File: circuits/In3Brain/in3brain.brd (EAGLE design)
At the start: 42.2 x 38.2 mm, 21 parts, among them IC1 ATMEGA48/88/168-AU, IC2 REG1117

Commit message: Electronics v2
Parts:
- removed LED: (no value), ng:1206
- removed R9: 0, ng:1206
- removed S1: (no value), ng:6MM_SWITCH
- removed SV2, SV3: (no value), con-lstb:MA06-1
- added J1: JACK.65MM, 01_fab:JACK_.65MM
- added SV5, SV6: (no value), con-lstb:MA05-2
- R1: value 10k -> 0
- R2: value 499 -> 0
- SL1: device con-amp-quick:02PA -> con-amp-quick:05PA
- moved R8 48.7 mm to (49.9, 59.4), turned to 0 degrees
- moved R4 44.2 mm to (43.3, 59.6)
- moved SL1 41.1 mm to (40.3, 66.1)
- moved C2 39.9 mm to (55.6, 45.5), turned to 0 degrees
- moved R3 39.6 mm to (41.7, 62.5), turned to 180 degrees
- moved R7 38.5 mm to (55.7, 41.2)
- moved U$1 37.5 mm to (53.2, 35.3)
- moved C5 36.4 mm to (35.5, 60.2), turned to 270 degrees
- moved IC1 35.9 mm to (40.6, 43.2)
- moved U$2 35.2 mm to (31.7, 39.4)
- moved C1 33.4 mm to (32.6, 60.0), turned to 270 degrees
- moved R2 31.2 mm to (28.7, 35.9)
- moved R1 25.5 mm to (41.5, 25.5), turned to 90 degrees
- moved C3 21.5 mm to (28.6, 30.6), turned to 0 degrees
- moved C6 17.3 mm to (28.6, 27.7), turned to 0 degrees
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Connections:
- removed net EN: SV2.1
- removed net N$23: LED.1, R2.2
- new net $1: SV5.5
- new net $2: SV5.6
- new net BTN: IC1.2, SV5.4
- new net BUZZ: IC1.12, SV6.2
- new net INT0: IC1.32, SV5.1
- new net INT1: IC1.1, SV5.2
- new net LCD4: IC1.23, SV5.8
- new net LCD5: IC1.24, SV5.10
- new net LCD6: IC1.25, SV5.9
- new net LCD7: IC1.26, SV5.7
- new net LCDE: IC1.10, SV6.3
- new net LCDRS: IC1.11, SV6.1
- new net RGBB: IC1.14, SV6.6
- new net RGBG: IC1.13, SV6.4
- net 12V: now also J1.PIN, SL1.4; no longer SL1.1, SV3.4
- net 5V: now also R2.1, R2.2, SV6.10, SV6.7; no longer R1.2, R9.1, R9.2, SV2.2, SV3.5
- net GND: now also J1.CONTACT, J1.SHUNT, R1.1, R1.2, SL1.5, SV6.5; no longer LED.2, S1.1, S1.2, SL1.2, SV2.3, SV3.6
- net RST: now also SL1.1, SV5.3, SV6.9; no longer R1.1, S1.3, S1.4, SV3.1
- net RX: no longer SV2.6
- net SCK: now also SV6.8; no longer R2.1
- net SCL: now also SL1.3; no longer SV3.3
- net SDA: now also SL1.2; no longer SV3.2
- net STATE: now also IC1.9; no longer IC1.2, SV2.4
- net TX: no longer SV2.5
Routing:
- net GND: track 119.2 -> 154.0 mm
- net 12V: track 58.7 -> 29.1 mm
- net N$23: track 28.7 -> 0.00 mm
- net SCK: track 18.0 -> 46.6 mm
- net BTN: track 0.00 -> 23.1 mm
- net LCD4: track 0.00 -> 22.8 mm
- net LCDE: track 0.00 -> 19.9 mm
- net N$3: track 18.5 -> 0.00 mm
- net RST: track 50.3 -> 68.1 mm
- net RX: track 15.5 -> 0.00 mm
- net SDA: track 35.2 -> 20.3 mm
- net TX: track 14.4 -> 0.00 mm
- net LCDRS: track 0.00 -> 14.1 mm
- net LCD5: track 0.00 -> 13.8 mm
- net INT1: track 0.00 -> 13.8 mm
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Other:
- board size 42.2 x 38.2 mm -> 40.2 x 47.7 mm
- board text removed: "+"
- board text removed: "-"
- board text removed: "3"
- board text removed: "In"

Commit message: New Electronics
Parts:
- removed J1: JACK.65MM, 01_fab:JACK_.65MM
- removed R7, R8: 0, ng:1206
- removed SV5: (no value), con-lstb:MA05-2
- added J2: (no value), con-jack:SPC4078
- added R5: 0, ng:1206
- added SL2, SL3: (no value), con-amp-quick:03P
- added SL5: (no value), con-amp-quick:07PA
- moved C5 60.1 mm to (5.59, 8.13), turned to 180 degrees
- moved C2 51.8 mm to (6.10, 30.5)
- moved SL1 50.0 mm to (38.1, 16.2), turned to 90 degrees
- moved R4 39.6 mm to (23.3, 25.3)
- moved R3 37.6 mm to (21.2, 31.0), turned to 270 degrees
- moved IC1 37.2 mm to (16.0, 15.2)
- moved U$2 36.5 mm to (7.09, 12.4)
- moved U$1 34.7 mm to (32.1, 7.70)
- moved R1 28.5 mm to (21.3, 5.33)
- moved SV6 25.1 mm to (16.3, 29.5), turned to 90 degrees
- moved C1 25.1 mm to (23.2, 36.8), turned to 0 degrees
- moved R2 24.5 mm to (25.9, 11.5), turned to 270 degrees
- moved C3 22.7 mm to (6.10, 27.4)
- moved C6 22.7 mm to (6.10, 24.6)
- moved IC2 15.7 mm to (28.5, 32.0), turned to 270 degrees
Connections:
- removed net $1: SV5.5
- removed net $2: SV5.6
- removed net LCD4: IC1.23, SV5.8
- removed net LCD5: IC1.24, SV5.10
- removed net LCD6: IC1.25, SV5.9
- removed net LCD7: IC1.26, SV5.7
- removed net LCDE: IC1.10, SV6.3
- removed net LCDRS: IC1.11, SV6.1
- removed net RGBB: IC1.14, SV6.6
- removed net RGBG: IC1.13, SV6.4
- removed net RX: IC1.30
- removed net STATE: IC1.9
- removed net TX: IC1.31
- new net FAN12: IC1.9, SL5.5
- new net FAN5: IC1.10, SL5.4
- new net LED: IC1.2, SV6.10
- new net PUMP: IC1.13, SL5.1
- new net RELAY1: IC1.11, SL5.3
- new net RELAY2: IC1.12, SL5.2
- new net TEMP1: IC1.23, SL2.1
- new net TEMP2: IC1.24, SL3.1
- net 12V: now also J2.3, SL1.5, SL5.7; no longer J1.PIN, SL1.4
- net 5V: now also SL2.3, SL3.3; no longer R8.1, R8.2, SV6.10
- net BTN: now also IC1.31, SV6.4; no longer IC1.2, SV5.4
- net BUZZ: now also IC1.30; no longer IC1.12
- net GND: now also J2.1, J2.2, R5.1, R5.2, SL1.2, SL2.2, SL3.2, SL5.6, SV6.9; no longer J1.CONTACT, J1.SHUNT, R1.1, R1.2, SL1.5, SV6.5
- net INT0: now also IC1.1, SV6.8; no longer IC1.32, SV5.1
- net INT1: now also IC1.32, SV6.6; no longer IC1.1, SV5.2
- net MISO: now also R1.1, R1.2
- net RST: now also IC1.19, SV6.1; no longer R7.1, R7.2, SV5.3, SV6.9
- net SCK: no longer SV6.8
- net SCL: now also SV6.3
- net SDA: now also SL1.4, SV6.5; no longer SL1.2
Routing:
- net GND: track 154.0 -> 0.00 mm
- net 12V: track 29.1 -> 111.4 mm
- net 5V: track 157.2 -> 98.2 mm
- net RST: track 68.1 -> 34.7 mm
- net SCK: track 46.6 -> 16.8 mm
- net SCL: track 19.7 -> 43.1 mm
- net LCD4: track 22.8 -> 0.00 mm
- net LED: track 0.00 -> 22.2 mm
- net SDA: track 20.3 -> 42.5 mm
- net LCDE: track 19.9 -> 0.00 mm
- net TEMP2: track 0.00 -> 15.9 mm
- net BTN: track 23.1 -> 8.37 mm
- net LCDRS: track 14.1 -> 0.00 mm
- net LCD5: track 13.8 -> 0.00 mm
- net MOSI: track 11.5 -> 24.5 mm
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- added copper zone on layer 1, net GND
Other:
- board size 40.2 x 47.7 mm -> 50.5 x 46.5 mm

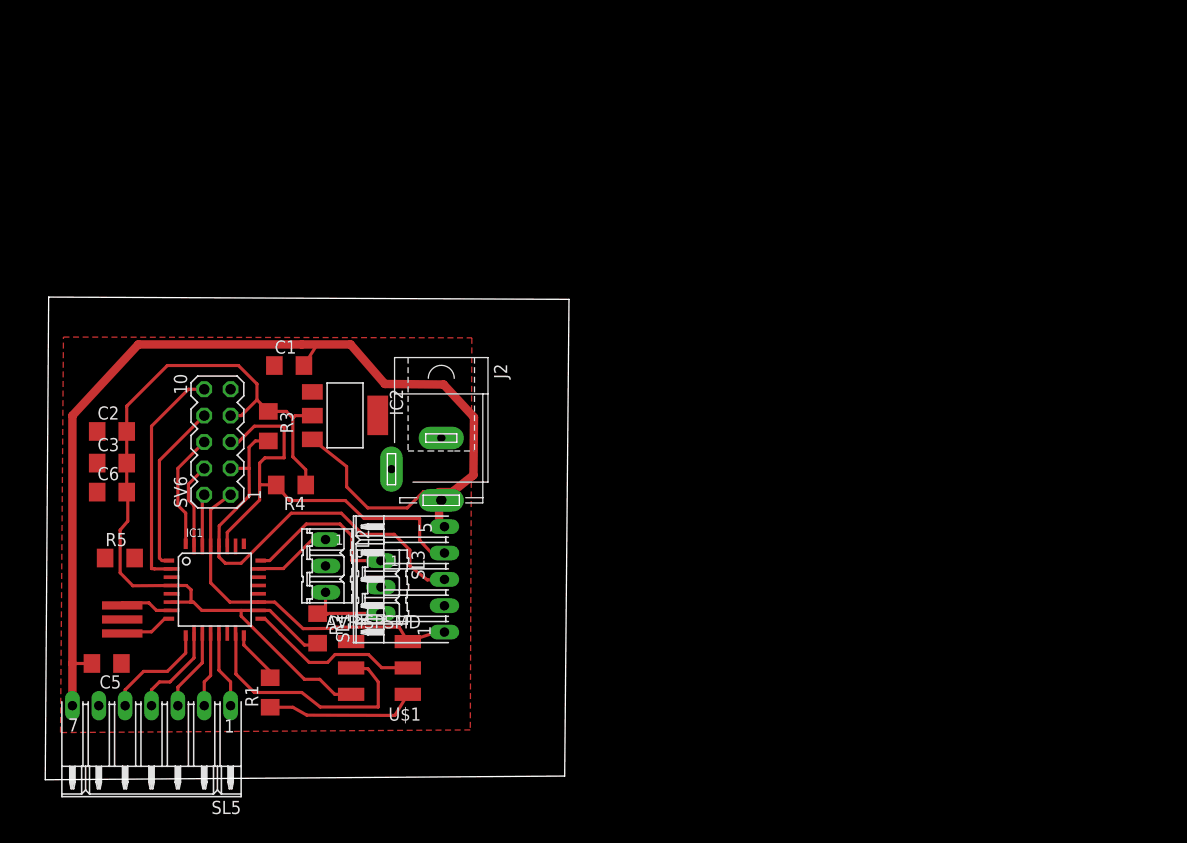
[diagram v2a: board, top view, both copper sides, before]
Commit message: new electronics: less components, less bards, space optimization and some software error fixes
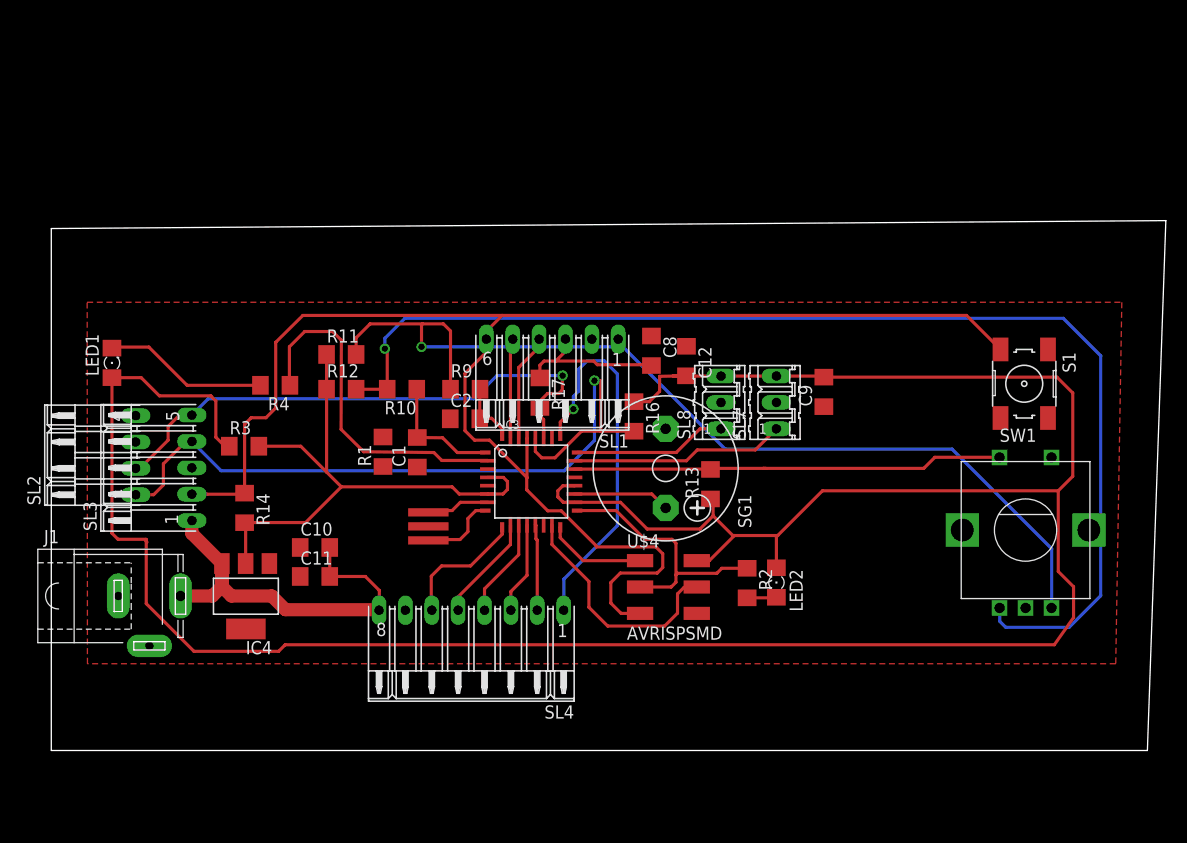
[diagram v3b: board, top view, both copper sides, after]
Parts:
- removed C3: .1uf, ng:1206
- removed C5, C6: 10uf, ng:1206
- removed IC1: ATMEGA48/88/168-AU, atmega8:TQFP32-08
- removed IC2: REG1117, burr-brown:SOT223
- removed J2: (no value), con-jack:SPC4078
- removed R5: 0, ng:1206
- removed SL5: (no value), con-amp-quick:07PA
- removed SV6: (no value), con-lstb:MA05-2
- removed U$1: AVRISPSMD, 01_FAB_Hello:2X03SMD
- removed U$2: RESONATOREFOB, fab:EFOBM
- added C10, C9: .1uf, ng:1206
- added C11, C12: 10uf, ng:1206
- added C8: 1uf, ng:1206
- added IC3: ATMEGA48/88/168-AU, atmega8:TQFP32-08
- added IC4: REG1117, burr-brown:SOT223
- added J1: (no value), con-jack:SPC4078
- added LED1, LED2: (no value), eagle-ltspice:LED_1206
- added R10, R11, R12, R13, R14, R16, R17, R9: 10k, ng:1206
- added S1: (no value), 01_FAB_Hello:6MM_SWITCH
- added SG1: F/CM12P, buzzer:F/CM12P
- added SL4: (no value), con-amp-quick:08PA
- added SL7, SL8: (no value), con-amp-quick:03P
- added SW1: EC12E_SW, switch-alps:ALPS_EC12E_SW
- added U$3: RESONATOREFOB, fab:EFOBM
- added U$4: AVRISPSMD, 01_FAB_Hello:2X03SMD
- C1: value .1uf -> 0.01uf; device ng:1206 -> 01_FAB_Hello:1206
- C2: value 1uf -> 0.01uf; device ng:1206 -> 01_FAB_Hello:1206
- R2: value 0 -> 499
- R3: value 10k -> 0
- R4: value 10k -> 499
- SL1: device con-amp-quick:05PA -> con-amp-quick:06PA
- SL2: device con-amp-quick:03P -> con-amp-quick:04PA
- SL3: device con-amp-quick:03P -> con-amp-quick:05PA
- moved R2 41.6 mm to (67.3, 15.9)
- moved C2 34.0 mm to (40.1, 31.7)
- moved R1 25.6 mm to (32.2, 28.5)
- moved SL1 25.4 mm to (48.5, 39.4), turned to 180 degrees
- moved SL3 21.5 mm to (13.8, 27.0), turned to 90 degrees
- moved SL2 21.2 mm to (8.38, 28.2), turned to 90 degrees
- moved C1 14.9 mm to (35.5, 28.5), turned to 90 degrees
- moved R4 9.72 mm to (21.8, 34.9)
- moved R3 3.03 mm to (18.8, 29.1), turned to 0 degrees
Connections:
- removed net AREF: IC1.20
- removed net N$9: IC1.7, U$2.3
- new net ADC2: IC3.25, SL4.1
- new net CTS: SL1.2
- new net N$2: LED2.C, R2.2
- new net N$3: IC3.8, U$3.1
- new net N$4: IC3.7, U$3.3
- new net N$5: R11.2, R9.1, SW1.B
- new net N$8: R10.2, R12.2, SW1.A
- new net RX: IC3.30, SL1.4
- new net TX: IC3.31, SL1.5
- net 12V: now also C10.2, C11.2, IC4.3, J1.3, SL3.1, SL4.8; no longer C1.2, C5.2, IC2.3, J2.3, SL1.5, SL5.7
- net 5V: now also C12.2, C8.2, C9.2, IC3.18, IC3.20, IC3.4, IC3.6, IC4.2, LED1.A, LED2.A, R11.1, R12.1, R13.1, R14.2, R16.1, R17.1, R3.2, SL1.3, SL7.3, SL8.3, U$4.2; no longer C2.2, C3.2, C6.2, IC1.18, IC1.4, IC1.6, IC2.2, R2.1, R2.2, R4.1, SL3.3, SV6.7, U$1.2
- net BTN: now also IC3.22, R13.2, SW1.D; no longer IC1.31, SV6.4
- net BUZZ: now also IC3.19, SG1.+; no longer IC1.30, SV6.2
- net FAN12: now also IC3.9, SL4.6; no longer IC1.9, SL5.5
- net FAN5: now also IC3.10, SL4.5; no longer IC1.10, SL5.4
- net GND: now also C10.1, C11.1, C12.1, C8.1, C9.1, IC3.21, IC3.3, IC3.5, IC4.1, J1.1, J1.2, R1.1, R1.2, S1.1, S1.2, SG1.-, SL1.1, SL2.4, SL3.3, SL4.7, SL7.2, SL8.2, SW1.C, SW1.E, U$3.2, U$4.6; no longer C3.1, C5.1, C6.1, IC1.21, IC1.3, IC1.5, IC2.1, J2.1, J2.2, R5.1, R5.2, SL1.2, SL2.2, SL3.2, SL5.6, SV6.9, U$1.6, U$2.2
- net INT0: now also C1.2, IC3.1, R10.1; no longer IC1.1, SV6.8
- net INT1: now also C2.2, IC3.32, R9.2; no longer IC1.32, SV6.6
- net LED: now also IC3.2, R4.1; no longer IC1.2, SV6.10
- net MISO: now also IC3.16, U$4.1; no longer IC1.16, R1.1, R1.2, U$1.1
- net MOSI: now also IC3.15, U$4.4; no longer IC1.15, U$1.4
- net N$1: now also LED1.C, R4.2; no longer IC1.8, U$2.1
- net PUMP: now also IC3.13, SL4.2; no longer IC1.13, SL5.1
- net RELAY1: now also IC3.11, SL4.4; no longer IC1.11, SL5.3
- net RELAY2: now also IC3.12, SL4.3; no longer IC1.12, SL5.2
- net RST: now also IC3.29, R14.1, S1.3, S1.4, SL1.6, SL3.2, U$4.5; no longer IC1.19, IC1.29, SL1.1, SV6.1, U$1.5
- net SCK: now also IC3.17, R2.1, U$4.3; no longer IC1.17, U$1.3
- net SCL: now also IC3.28, R16.2, SL2.1, SL3.4; no longer IC1.28, R3.2, SL1.3, SV6.3
- net SDA: now also IC3.27, R17.2, SL2.2, SL3.5; no longer IC1.27, R4.2, SL1.4, SV6.5
- net TEMP1: now also IC3.23, SL7.1; no longer IC1.23, SL2.1
- net TEMP2: now also IC3.24, SL8.1; no longer IC1.24, SL3.1
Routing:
- net 5V: track 98.2 -> 340.6 mm
- net N$8: track 0.00 -> 114.9 mm, vias 0 -> 1
- net RST: track 34.7 -> 148.7 mm
- net N$5: track 0.00 -> 94.1 mm, vias 0 -> 1
- net 12V: track 111.4 -> 40.3 mm
- net ADC2: track 0.00 -> 36.6 mm, vias 0 -> 1
- net BTN: track 8.37 -> 41.7 mm
- net SCL: track 43.1 -> 74.0 mm, vias 0 -> 1
- net TEMP1: track 7.67 -> 20.7 mm
- net LED: track 22.2 -> 33.6 mm
- net SDA: track 42.5 -> 53.9 mm, vias 0 -> 1
- net N$1: track 5.11 -> 15.9 mm
- net TX: track 0.00 -> 10.7 mm
- net RX: track 0.00 -> 10.4 mm
- net MISO: track 19.7 -> 9.60 mm
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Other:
- board size 50.5 x 46.5 mm -> 107.4 x 51 mm
